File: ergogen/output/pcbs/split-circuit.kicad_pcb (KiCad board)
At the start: 2 copper layers, 137.5 x 95.8 mm, 44 parts

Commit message: feat/file-cleanup
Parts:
- removed B1: , E73:SW_TACT_ALPS_SKQGABE010
- added PWR1: , ceoloide:power_switch_smd_side, F.Cu at (263.0, 145.0)
- MCU1: footprint ProMicro -> ceoloide:mcu_nice_nano
- turned MCU1 to 0 degrees
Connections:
- net P0 renamed MCU1_14
- net P1 renamed MCU1_13
- net P2 renamed MCU1_17
- net P3 renamed MCU1_18
- net P4 renamed MCU1_19
- net P5 renamed MCU1_20
- net P6 renamed MCU1_21
- net P7 renamed MCU1_22
- net P8 renamed MCU1_23
- net P9 renamed MCU1_24
- MCU1 pad 1: RAW -> MCU1_1
- MCU1 pad 10: P14 -> MCU1_10
- MCU1 pad 11: P16 -> MCU1_11
- MCU1 pad 12: P10 -> MCU1_12
- MCU1 pad 15: GND -> MCU1_15
- MCU1 pad 16: GND -> MCU1_16
- MCU1 pad 2: GND -> MCU1_2
- MCU1 pad 3: RST -> MCU1_3
- MCU1 pad 4: VCC -> MCU1_4
- MCU1 pad 5: P21 -> MCU1_5
- MCU1 pad 6: P20 -> MCU1_6
- MCU1 pad 7: P19 -> MCU1_7
- MCU1 pad 8: P18 -> MCU1_8
- MCU1 pad 9: P15 -> MCU1_9
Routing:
- net (no net): track 0.00 -> 337.7 mm
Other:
- net class Default removed

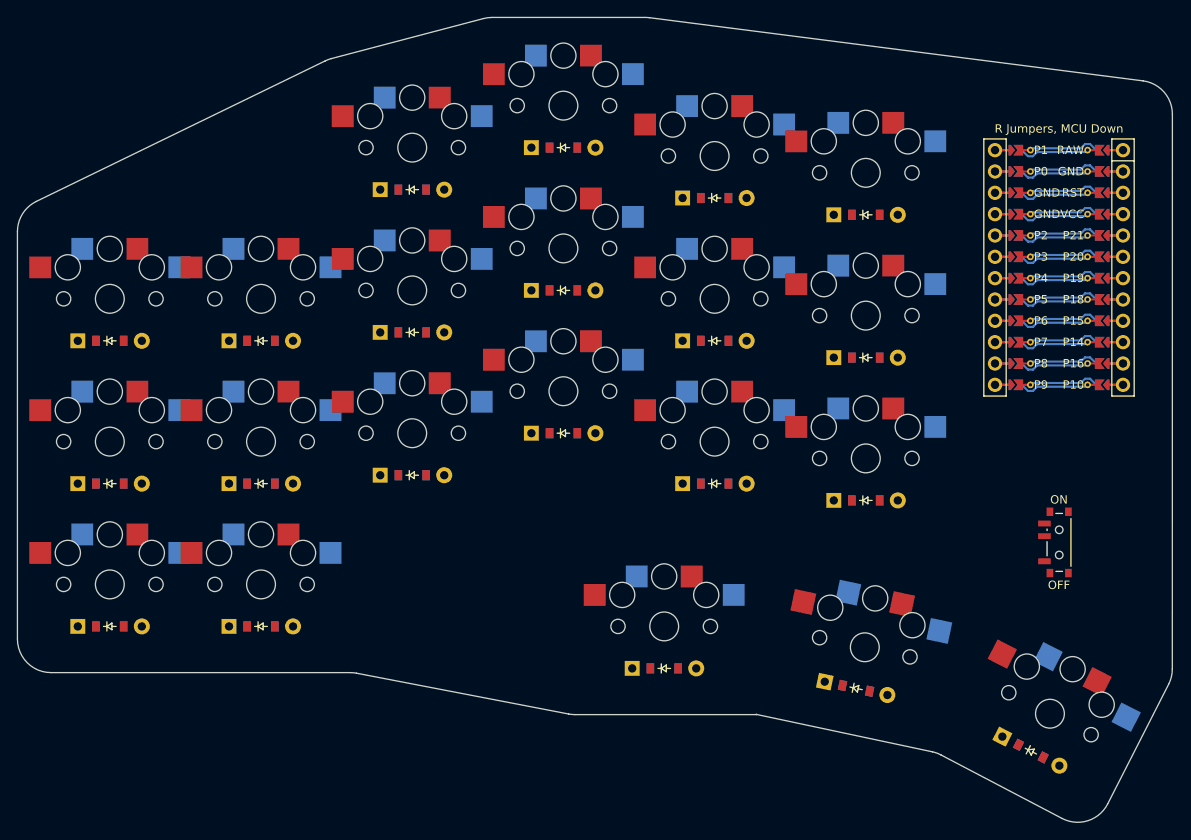
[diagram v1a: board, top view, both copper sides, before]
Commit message: feat/update-ergogen-config-file-and-generate-pcb
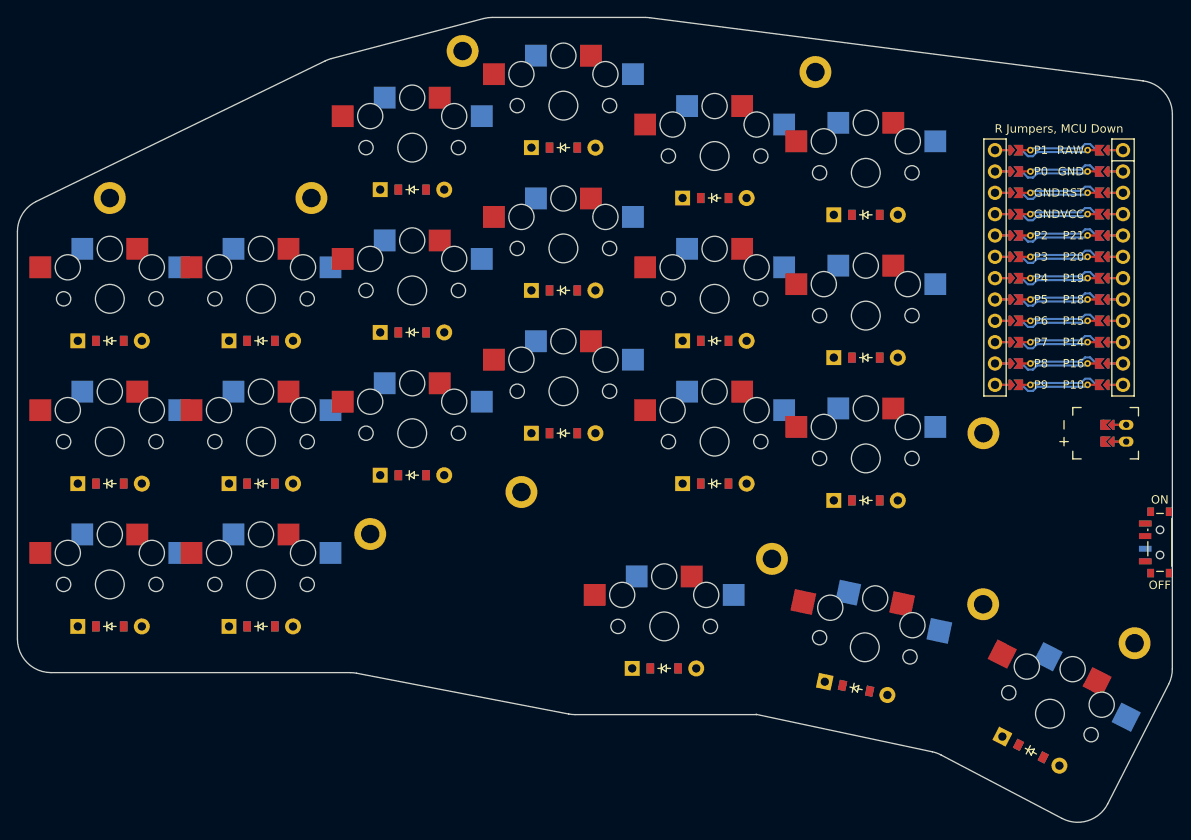
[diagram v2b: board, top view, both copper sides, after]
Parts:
- added H1: , ceoloide:mounting_hole_plated, F.Cu at (234.0, 89.0)
- added H10: , ceoloide:mounting_hole_plated, F.Cu at (150.0, 104.0)
- added H2: , ceoloide:mounting_hole_plated, F.Cu at (254.0, 132.0)
- added H3: , ceoloide:mounting_hole_plated, F.Cu at (272.0, 157.0)
- added H4: , ceoloide:mounting_hole_plated, F.Cu at (254.0, 152.4)
- added H5: , ceoloide:mounting_hole_plated, F.Cu at (228.8, 147.0)
- added H6: , ceoloide:mounting_hole_plated, F.Cu at (181.0, 144.0)
- added H7: , ceoloide:mounting_hole_plated, F.Cu at (199.0, 139.0)
- added H8: , ceoloide:mounting_hole_plated, F.Cu at (192.0, 86.5)
- added H9: , ceoloide:mounting_hole_plated, F.Cu at (174.0, 104.0)
- added JST1: , ceoloide:battery_connector_jst_ph_2, F.Cu at (271.0, 132.0)
- moved PWR1 12.0 mm to (275.0, 145.0)
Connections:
- D1 pad 1: (no net) -> P14
- D10 pad 1: (no net) -> P14
- D11 pad 1: (no net) -> P16
- D12 pad 1: (no net) -> P10
- D13 pad 1: (no net) -> P14
- D14 pad 1: (no net) -> P16
- D15 pad 1: (no net) -> P10
- D16 pad 1: (no net) -> P14
- D17 pad 1: (no net) -> P16
- D18 pad 1: (no net) -> P10
- D19 pad 1: (no net) -> P15
- D2 pad 1: (no net) -> P16
- D20 pad 1: (no net) -> P15
- D21 pad 1: (no net) -> P15
- D3 pad 1: (no net) -> P10
- D4 pad 1: (no net) -> P14
- D5 pad 1: (no net) -> P16
- D6 pad 1: (no net) -> P10
- D7 pad 1: (no net) -> P14
- D8 pad 1: (no net) -> P16
- D9 pad 1: (no net) -> P10
- PWR1 pad 1: (no net) -> BAT_P
- PWR1 pad 3: GND -> BAT_P
- S1 pad 1: (no net) -> P9
- S10 pad 1: (no net) -> P6
- S11 pad 1: (no net) -> P6
- S12 pad 1: (no net) -> P6
- S13 pad 1: (no net) -> P5
- S14 pad 1: (no net) -> P5
- S15 pad 1: (no net) -> P5
- S16 pad 1: (no net) -> P4
- S17 pad 1: (no net) -> P4
- S18 pad 1: (no net) -> P4
- S19 pad 1: (no net) -> P6
- S2 pad 1: (no net) -> P9
- S20 pad 1: (no net) -> P5
- S21 pad 1: (no net) -> P4
- S3 pad 1: (no net) -> P9
- S4 pad 1: (no net) -> P8
- S5 pad 1: (no net) -> P8
- S6 pad 1: (no net) -> P8
- S7 pad 1: (no net) -> P7
- S8 pad 1: (no net) -> P7
- S9 pad 1: (no net) -> P7
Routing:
- net JST1_2: track 0.00 -> 3.60 mm
- net JST1_1: track 0.00 -> 3.60 mm
